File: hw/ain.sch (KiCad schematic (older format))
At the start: 3 parts

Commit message: hw 1.0 ready to order
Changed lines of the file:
@@
 $Descr A4 11693 8268
 encoding utf-8
-Sheet 11 13
+Sheet 14 14
 Title ""
 Date ""
@@
 AR Path="/5A7E2A6E/5A7E0603" Ref="R1201"  Part="1"
 AR Path="/5A7E34BA/5A7E0603" Ref="R1301"  Part="1"
-F 0 "R1101" V 5408 4008 45  0000 L CNN
+AR Path="/5A8C5348/5A7E0603" Ref="R1401"  Part="1"
+F 0 "R1401" V 5408 4008 45  0000 L CNN
 F 1 "10K" V 5492 4008 45  0000 L CNN
 F 2 "yageo:0603" H 5430 4100 20  0001 C CNN
@@
 AR Path="/5A7E2A6E/5A7E064B" Ref="R1202"  Part="1"
 AR Path="/5A7E34BA/5A7E064B" Ref="R1302"  Part="1"
-F 0 "R1102" V 5408 4408 45  0000 L CNN
+AR Path="/5A8C5348/5A7E064B" Ref="R1402"  Part="1"
+F 0 "R1402" V 5408 4408 45  0000 L CNN
 F 1 "20K" V 5492 4408 45  0000 L CNN
 F 2 "yageo:0603" H 5430 4500 20  0001 C CNN
@@
 AR Path="/5A7E2A6E/5A7E069C" Ref="D1201"  Part="1"
 AR Path="/5A7E34BA/5A7E069C" Ref="D1301"  Part="1"
-F 0 "D1101" V 5700 3802 45  0000 R CNN
+AR Path="/5A8C5348/5A7E069C" Ref="D1401"  Part="1"
+F 0 "D1401" V 5700 3802 45  0000 R CNN
 F 1 "DIODE_RS07J-GS18" H 5770 3840 45  0001 L BNN
 F 2 "usevolt:DO219AB" H 5780 4050 20  0001 C CNN
@@
 $EndComp
 $Comp
-L +3V3 #PWR1102
+L +3V3 #PWR049
 U 1 1 5A7E070C
 P 5750 3750
-AR Path="/5A7E031E/5A7E070C" Ref="#PWR1102"  Part="1"
-AR Path="/5A7E2A6E/5A7E070C" Ref="#PWR1202"  Part="1"
-AR Path="/5A7E34BA/5A7E070C" Ref="#PWR1302"  Part="1"
-F 0 "#PWR1102" H 5750 3600 50  0001 C CNN
+AR Path="/5A7E031E/5A7E070C" Ref="#PWR049"  Part="1"
+AR Path="/5A7E2A6E/5A7E070C" Ref="#PWR051"  Part="1"
+AR Path="/5A7E34BA/5A7E070C" Ref="#PWR053"  Part="1"
+AR Path="/5A8C5348/5A7E070C" Ref="#PWR055"  Part="1"
+F 0 "#PWR055" H 5750 3600 50  0001 C CNN
 F 1 "+3V3" H 5765 3923 50  0000 C CNN
 F 2 "" H 5750 3750 50  0000 C CNN
@@
 	5400 4150 5400 4250
 $Comp
-L GND #PWR1101
+L GND #PWR050
 U 1 1 5A7E07A0
 P 5400 4600
-AR Path="/5A7E031E/5A7E07A0" Ref="#PWR1101"  Part="1"
-AR Path="/5A7E2A6E/5A7E07A0" Ref="#PWR1201"  Part="1"
-AR Path="/5A7E34BA/5A7E07A0" Ref="#PWR1301"  Part="1"
-F 0 "#PWR1101" H 5400 4350 50  0001 C CNN
+AR Path="/5A7E031E/5A7E07A0" Ref="#PWR050"  Part="1"
+AR Path="/5A7E2A6E/5A7E07A0" Ref="#PWR052"  Part="1"
+AR Path="/5A7E34BA/5A7E07A0" Ref="#PWR054"  Part="1"
+AR Path="/5A8C5348/5A7E07A0" Ref="#PWR056"  Part="1"
+F 0 "#PWR056" H 5400 4350 50  0001 C CNN
 F 1 "GND" H 5405 4427 50  0000 C CNN
 F 2 "" H 5400 4600 50  0000 C CNN

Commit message: 050518: Kikepera head prototype first revision, saw not working
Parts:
- D1101: symbol DIODE_RS07J-GS18 -> icu-rescue:DIODE_RS07J-GS18
- R1101: symbol 10K -> icu-rescue:10K
- R1102: symbol 20K -> icu-rescue:20K
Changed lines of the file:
@@
-EESchema Schematic File Version 2
-LIBS:kemet
-LIBS:usevolt
-LIBS:wurth_elektronik_LED
-LIBS:power
-LIBS:yageo
+EESchema Schematic File Version 4
 LIBS:icu-cache
 EELAYER 26 0
@@
 VIN
 $Comp
-L 10K R1101
+L icu-rescue:10K R1101
 U 1 1 5A7E0603
 P 5400 3950
@@
 $EndComp
 $Comp
-L 20K R1102
+L icu-rescue:20K R1102
 U 1 1 5A7E064B
 P 5400 4350
@@
 $EndComp
 $Comp
-L DIODE_RS07J-GS18 D1101
+L icu-rescue:DIODE_RS07J-GS18 D1101
 U 1 1 5A7E069C
 P 5750 3900
@@
 $EndComp
 $Comp
-L +3V3 #PWR049
+L icu-rescue:+3V3 #PWR049
 U 1 1 5A7E070C
 P 5750 3750
@@
 AR Path="/5A7E34BA/5A7E070C" Ref="#PWR053"  Part="1"
 AR Path="/5A8C5348/5A7E070C" Ref="#PWR055"  Part="1"
+AR Path="/5A7E070C" Ref="#PWR055"  Part="1"
 F 0 "#PWR055" H 5750 3600 50  0001 C CNN
 F 1 "+3V3" H 5765 3923 50  0000 C CNN
@@
 	5400 4150 5400 4250
 $Comp
-L GND #PWR050
+L icu-rescue:GND #PWR050
 U 1 1 5A7E07A0
 P 5400 4600

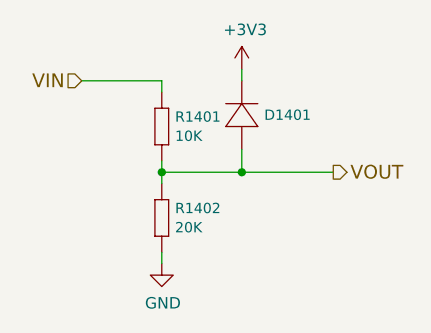
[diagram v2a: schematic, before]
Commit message: 2 din replaced with ain, zeners added to outputs
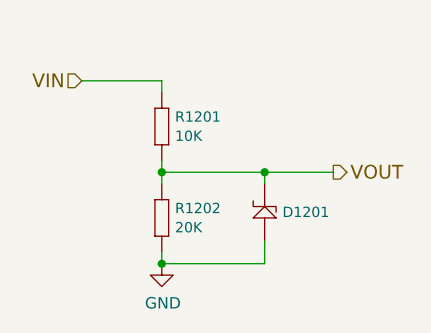
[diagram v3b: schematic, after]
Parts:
- removed D1101: DIODE_RS07J-GS18, usevolt:DO219AB, symbol icu-rescue:DIODE_RS07J-GS18
- added D1201: ZENER_MM3Z3V6T1G, usevolt:SOD-323, symbol usevolt:ZENER_MM3Z3V6T1G
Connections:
- net GND: now also D1201.2
- net VOUT: now also D1201.1
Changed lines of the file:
@@
 $Descr A4 11693 8268
 encoding utf-8
-Sheet 14 14
+Sheet 13 13
 Title ""
 Date ""
@@
 AR Path="/5A7E34BA/5A7E0603" Ref="R1301"  Part="1"
 AR Path="/5A8C5348/5A7E0603" Ref="R1401"  Part="1"
-F 0 "R1401" V 5408 4008 45  0000 L CNN
+AR Path="/5B70DDCB/5A7E0603" Ref="R1201"  Part="1"
+AR Path="/5B73B713/5A7E0603" Ref="R1301"  Part="1"
+F 0 "R1201" V 5408 4008 45  0000 L CNN
 F 1 "10K" V 5492 4008 45  0000 L CNN
 F 2 "yageo:0603" H 5430 4100 20  0001 C CNN
@@
 AR Path="/5A7E34BA/5A7E064B" Ref="R1302"  Part="1"
 AR Path="/5A8C5348/5A7E064B" Ref="R1402"  Part="1"
-F 0 "R1402" V 5408 4408 45  0000 L CNN
+AR Path="/5B70DDCB/5A7E064B" Ref="R1202"  Part="1"
+AR Path="/5B73B713/5A7E064B" Ref="R1302"  Part="1"
+F 0 "R1202" V 5408 4408 45  0000 L CNN
 F 1 "20K" V 5492 4408 45  0000 L CNN
 F 2 "yageo:0603" H 5430 4500 20  0001 C CNN
@@
 	0    1    1    0
 $EndComp
-$Comp
-L icu-rescue:DIODE_RS07J-GS18 D1101
-U 1 1 5A7E069C
-P 5750 3900
-AR Path="/5A7E031E/5A7E069C" Ref="D1101"  Part="1"
-AR Path="/5A7E2A6E/5A7E069C" Ref="D1201"  Part="1"
-AR Path="/5A7E34BA/5A7E069C" Ref="D1301"  Part="1"
-AR Path="/5A8C5348/5A7E069C" Ref="D1401"  Part="1"
-F 0 "D1401" V 5700 3802 45  0000 R CNN
-F 1 "DIODE_RS07J-GS18" H 5770 3840 45  0001 L BNN
-F 2 "usevolt:DO219AB" H 5780 4050 20  0001 C CNN
-F 3 "http://www.vishay.com/docs/85742/rs07b.pdf" H 5770 3920 60  0001 C CNN
-F 4 "1864882" H 6370 4520 60  0001 C CNN "2nd Source Part Number"
-F 5 "Digi-Key" H 6070 4220 60  0001 C CNN "1st Source"
-F 6 "Farnell" H 6270 4420 60  0001 C CNN "2nd Source"
-F 7 "RS07J-GS18" H 5970 4120 60  0001 C CNN "Manufacturer Part Number"
-F 8 "RS07J-GS18-ND" H 6170 4320 60  0001 C CNN "1st Source Part Number"
-F 9 "Vishay Semiconductor Diodes Division" H 5870 4020 60  0001 C CNN "Manufacturer"
-	1    5750 3900
-	0    -1   -1   0
-$EndComp
-$Comp
-L icu-rescue:+3V3 #PWR049
-U 1 1 5A7E070C
-P 5750 3750
-AR Path="/5A7E031E/5A7E070C" Ref="#PWR049"  Part="1"
-AR Path="/5A7E2A6E/5A7E070C" Ref="#PWR051"  Part="1"
-AR Path="/5A7E34BA/5A7E070C" Ref="#PWR053"  Part="1"
-AR Path="/5A8C5348/5A7E070C" Ref="#PWR055"  Part="1"
-AR Path="/5A7E070C" Ref="#PWR055"  Part="1"
-F 0 "#PWR055" H 5750 3600 50  0001 C CNN
-F 1 "+3V3" H 5765 3923 50  0000 C CNN
-F 2 "" H 5750 3750 50  0000 C CNN
-F 3 "" H 5750 3750 50  0000 C CNN
-	1    5750 3750
-	1    0    0    -1
-$EndComp
-Wire Wire Line
-	5750 3750 5750 3800
 Wire Wire Line
 	5400 3850 5400 3800
 Wire Wire Line
-	5400 4150 5400 4250
+	5400 4150 5400 4200
 $Comp
 L icu-rescue:GND #PWR050
@@
 AR Path="/5A7E34BA/5A7E07A0" Ref="#PWR054"  Part="1"
 AR Path="/5A8C5348/5A7E07A0" Ref="#PWR056"  Part="1"
-F 0 "#PWR056" H 5400 4350 50  0001 C CNN
+AR Path="/5B70DDCB/5A7E07A0" Ref="#PWR0104"  Part="1"
+AR Path="/5B73B713/5A7E07A0" Ref="#PWR0105"  Part="1"
+F 0 "#PWR0104" H 5400 4350 50  0001 C CNN
 F 1 "GND" H 5405 4427 50  0000 C CNN
 F 2 "" H 5400 4600 50  0000 C CNN
@@
 Wire Wire Line
 	5400 4600 5400 4550
-Wire Wire Line
-	5400 4200 6150 4200
 Connection ~ 5400 4200
 Wire Wire Line
 	5400 3800 5050 3800
 Wire Wire Line
-	5750 4100 5750 4200
-Connection ~ 5750 4200
+	5400 4200 5400 4250
+Wire Wire Line
+	5400 4200 5850 4200
+$Comp
+L usevolt:ZENER_MM3Z3V6T1G D1201
+U 1 1 5B70E023
+P 5850 4300
+AR Path="/5B70DDCB/5B70E023" Ref="D1201"  Part="1"
+AR Path="/5B73B713/5B70E023" Ref="D1301"  Part="1"
+F 0 "D1201" V 5775 4222 45  0000 R CNN
+F 1 "ZENER_MM3Z3V6T1G" H 6125 4675 45  0001 L BNN
+F 2 "usevolt:SOD-323" H 5825 4675 20  0001 C CNN
+F 3 "http://www.mouser.com/ds/2/308/MM3Z2V4T1-D-269162.pdf" H 6200 4875 60  0001 C CNN
+F 4 "Mouser" H 6170 4620 60  0001 C CNN "1st Source"
+F 5 "MM3Z3V6T1G" H 6070 4520 60  0001 C CNN "Manufacturer Part Number"
+F 6 "863-MM3Z3V6T1G" H 6270 4720 60  0001 C CNN "1st Source Part Number"
+F 7 "ON Semiconductor" H 6125 4775 60  0001 C CNN "Manufacturer"
+	1    5850 4300
+	0    -1   -1   0
+$EndComp
+Wire Wire Line
+	5850 4250 5850 4200
+Connection ~ 5850 4200
+Wire Wire Line
+	5850 4200 6150 4200
+Wire Wire Line
+	5850 4500 5850 4600
+Wire Wire Line
+	5850 4600 5400 4600
+Connection ~ 5400 4600
 $EndSCHEMATC

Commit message: CM_6.2.1 delivered, first customer machine with CCU, HCU & ICU
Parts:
- removed D1201: ZENER_MM3Z3V6T1G, usevolt:SOD-323, symbol usevolt:ZENER_MM3Z3V6T1G
- added D1101: DIODE_RS07J-GS18, usevolt:DO219AB, symbol DIODE_RS07J-GS18
- R1101: symbol icu-rescue:10K -> 10K
- R1102: symbol icu-rescue:20K -> 20K
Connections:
- net VOUT: now also D1101.P$1 (P)
- new net +3V3: D1101.P$2 (N)
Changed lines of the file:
@@
-EESchema Schematic File Version 4
+EESchema Schematic File Version 2
+LIBS:kemet
+LIBS:usevolt
+LIBS:wurth_elektronik_LED
+LIBS:power
+LIBS:yageo
 LIBS:icu-cache
 EELAYER 26 0
@@
 $Descr A4 11693 8268
 encoding utf-8
-Sheet 13 13
+Sheet 14 14
 Title ""
 Date ""
@@
 VIN
 $Comp
-L icu-rescue:10K R1101
+L 10K R1101
 U 1 1 5A7E0603
 P 5400 3950
@@
 AR Path="/5A7E34BA/5A7E0603" Ref="R1301"  Part="1"
 AR Path="/5A8C5348/5A7E0603" Ref="R1401"  Part="1"
-AR Path="/5B70DDCB/5A7E0603" Ref="R1201"  Part="1"
-AR Path="/5B73B713/5A7E0603" Ref="R1301"  Part="1"
-F 0 "R1201" V 5408 4008 45  0000 L CNN
+F 0 "R1401" V 5408 4008 45  0000 L CNN
 F 1 "10K" V 5492 4008 45  0000 L CNN
 F 2 "yageo:0603" H 5430 4100 20  0001 C CNN
@@
 $EndComp
 $Comp
-L icu-rescue:20K R1102
+L 20K R1102
 U 1 1 5A7E064B
 P 5400 4350
@@
 AR Path="/5A7E34BA/5A7E064B" Ref="R1302"  Part="1"
 AR Path="/5A8C5348/5A7E064B" Ref="R1402"  Part="1"
-AR Path="/5B70DDCB/5A7E064B" Ref="R1202"  Part="1"
-AR Path="/5B73B713/5A7E064B" Ref="R1302"  Part="1"
-F 0 "R1202" V 5408 4408 45  0000 L CNN
+F 0 "R1402" V 5408 4408 45  0000 L CNN
 F 1 "20K" V 5492 4408 45  0000 L CNN
 F 2 "yageo:0603" H 5430 4500 20  0001 C CNN
@@
 	0    1    1    0
 $EndComp
+$Comp
+L DIODE_RS07J-GS18 D1101
+U 1 1 5A7E069C
+P 5750 3900
+AR Path="/5A7E031E/5A7E069C" Ref="D1101"  Part="1"
+AR Path="/5A7E2A6E/5A7E069C" Ref="D1201"  Part="1"
+AR Path="/5A7E34BA/5A7E069C" Ref="D1301"  Part="1"
+AR Path="/5A8C5348/5A7E069C" Ref="D1401"  Part="1"
+F 0 "D1401" V 5700 3802 45  0000 R CNN
+F 1 "DIODE_RS07J-GS18" H 5770 3840 45  0001 L BNN
+F 2 "usevolt:DO219AB" H 5780 4050 20  0001 C CNN
+F 3 "http://www.vishay.com/docs/85742/rs07b.pdf" H 5770 3920 60  0001 C CNN
+F 4 "1864882" H 6370 4520 60  0001 C CNN "2nd Source Part Number"
+F 5 "Digi-Key" H 6070 4220 60  0001 C CNN "1st Source"
+F 6 "Farnell" H 6270 4420 60  0001 C CNN "2nd Source"
+F 7 "RS07J-GS18" H 5970 4120 60  0001 C CNN "Manufacturer Part Number"
+F 8 "RS07J-GS18-ND" H 6170 4320 60  0001 C CNN "1st Source Part Number"
+F 9 "Vishay Semiconductor Diodes Division" H 5870 4020 60  0001 C CNN "Manufacturer"
+	1    5750 3900
+	0    -1   -1   0
+$EndComp
+$Comp
+L +3V3 #PWR049
+U 1 1 5A7E070C
+P 5750 3750
+AR Path="/5A7E031E/5A7E070C" Ref="#PWR049"  Part="1"
+AR Path="/5A7E2A6E/5A7E070C" Ref="#PWR051"  Part="1"
+AR Path="/5A7E34BA/5A7E070C" Ref="#PWR053"  Part="1"
+AR Path="/5A8C5348/5A7E070C" Ref="#PWR055"  Part="1"
+F 0 "#PWR055" H 5750 3600 50  0001 C CNN
+F 1 "+3V3" H 5765 3923 50  0000 C CNN
+F 2 "" H 5750 3750 50  0000 C CNN
+F 3 "" H 5750 3750 50  0000 C CNN
+	1    5750 3750
+	1    0    0    -1
+$EndComp
+Wire Wire Line
+	5750 3750 5750 3800
 Wire Wire Line
 	5400 3850 5400 3800
 Wire Wire Line
-	5400 4150 5400 4200
+	5400 4150 5400 4250
 $Comp
-L icu-rescue:GND #PWR050
+L GND #PWR050
 U 1 1 5A7E07A0
 P 5400 4600
@@
 AR Path="/5A7E34BA/5A7E07A0" Ref="#PWR054"  Part="1"
 AR Path="/5A8C5348/5A7E07A0" Ref="#PWR056"  Part="1"
-AR Path="/5B70DDCB/5A7E07A0" Ref="#PWR0104"  Part="1"
-AR Path="/5B73B713/5A7E07A0" Ref="#PWR0105"  Part="1"
-F 0 "#PWR0104" H 5400 4350 50  0001 C CNN
+F 0 "#PWR056" H 5400 4350 50  0001 C CNN
 F 1 "GND" H 5405 4427 50  0000 C CNN
 F 2 "" H 5400 4600 50  0000 C CNN
@@
 Wire Wire Line
 	5400 4600 5400 4550
+Wire Wire Line
+	5400 4200 6150 4200
 Connection ~ 5400 4200
 Wire Wire Line
 	5400 3800 5050 3800
 Wire Wire Line
-	5400 4200 5400 4250
-Wire Wire Line
-	5400 4200 5850 4200
-$Comp
-L usevolt:ZENER_MM3Z3V6T1G D1201
-U 1 1 5B70E023
-P 5850 4300
-AR Path="/5B70DDCB/5B70E023" Ref="D1201"  Part="1"
-AR Path="/5B73B713/5B70E023" Ref="D1301"  Part="1"
-F 0 "D1201" V 5775 4222 45  0000 R CNN
-F 1 "ZENER_MM3Z3V6T1G" H 6125 4675 45  0001 L BNN
-F 2 "usevolt:SOD-323" H 5825 4675 20  0001 C CNN
-F 3 "http://www.mouser.com/ds/2/308/MM3Z2V4T1-D-269162.pdf" H 6200 4875 60  0001 C CNN
-F 4 "Mouser" H 6170 4620 60  0001 C CNN "1st Source"
-F 5 "MM3Z3V6T1G" H 6070 4520 60  0001 C CNN "Manufacturer Part Number"
-F 6 "863-MM3Z3V6T1G" H 6270 4720 60  0001 C CNN "1st Source Part Number"
-F 7 "ON Semiconductor" H 6125 4775 60  0001 C CNN "Manufacturer"
-	1    5850 4300
-	0    -1   -1   0
-$EndComp
-Wire Wire Line
-	5850 4250 5850 4200
-Connection ~ 5850 4200
-Wire Wire Line
-	5850 4200 6150 4200
-Wire Wire Line
-	5850 4500 5850 4600
-Wire Wire Line
-	5850 4600 5400 4600
-Connection ~ 5400 4600
+	5750 4100 5750 4200
+Connection ~ 5750 4200
 $EndSCHEMATC

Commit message: 3.0.0 hw and gerber created
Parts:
- D1101: symbol DIODE_RS07J-GS18 -> usevolt:DIODE_RS07J-GS18
- R1101: symbol 10K -> yageo:10K
- R1102: symbol 20K -> yageo:20K
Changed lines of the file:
@@
-EESchema Schematic File Version 2
-LIBS:kemet
-LIBS:usevolt
-LIBS:wurth_elektronik_LED
-LIBS:power
-LIBS:yageo
+EESchema Schematic File Version 4
 LIBS:icu-cache
 EELAYER 26 0
@@
 VIN
 $Comp
-L 10K R1101
+L yageo:10K R1101
 U 1 1 5A7E0603
 P 5400 3950
@@
 $EndComp
 $Comp
-L 20K R1102
+L yageo:20K R1102
 U 1 1 5A7E064B
 P 5400 4350
@@
 $EndComp
 $Comp
-L DIODE_RS07J-GS18 D1101
+L usevolt:DIODE_RS07J-GS18 D1101
 U 1 1 5A7E069C
 P 5750 3900
@@
 $EndComp
 $Comp
-L +3V3 #PWR049
+L power:+3V3 #PWR049
 U 1 1 5A7E070C
 P 5750 3750
@@
 	5400 4150 5400 4250
 $Comp
-L GND #PWR050
+L power:GND #PWR050
 U 1 1 5A7E07A0
 P 5400 4600
